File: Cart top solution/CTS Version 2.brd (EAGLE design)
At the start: 116.5 x 63 mm, 10 parts, among them T2 2N2222, U1 RASPBERRY_PI_40SMD, X1 CON-WAGO_740_740-102

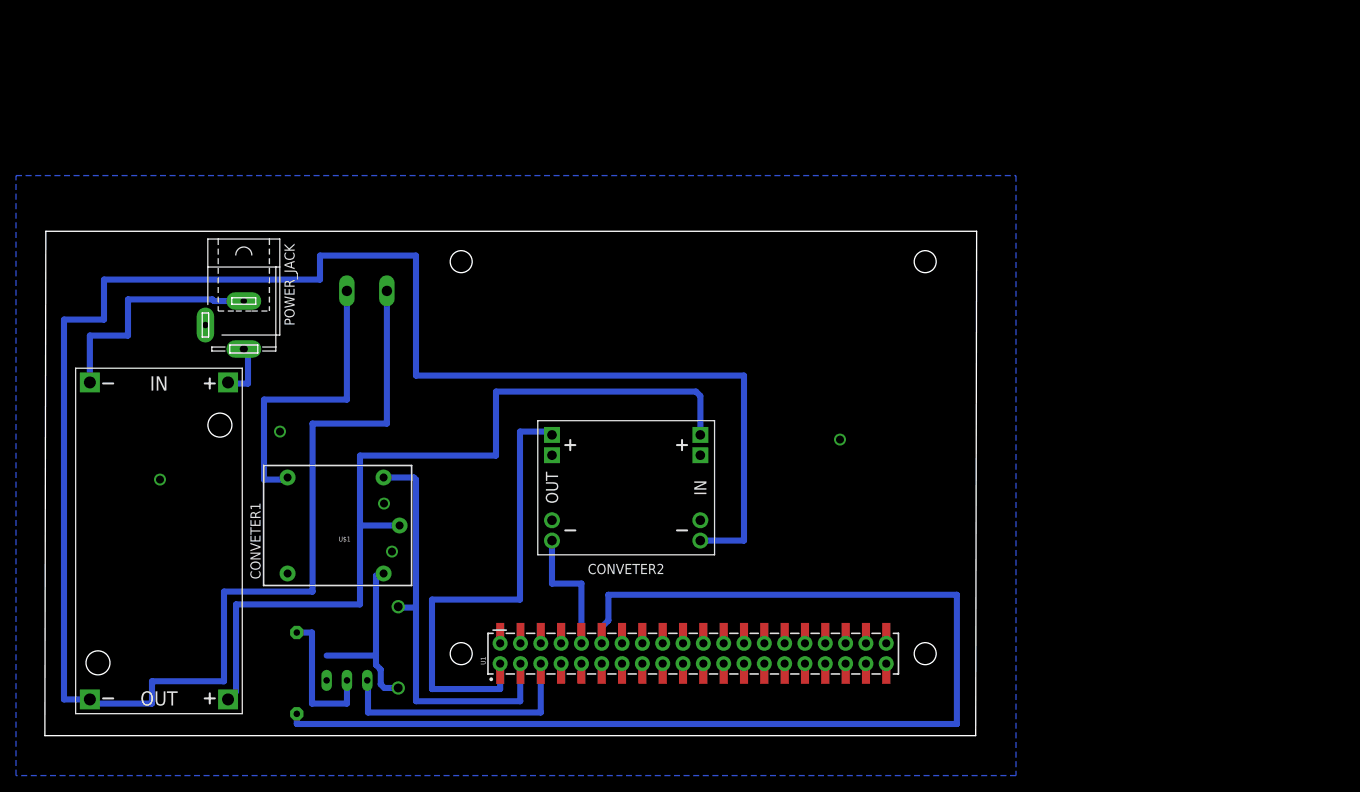
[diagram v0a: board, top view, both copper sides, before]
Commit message: Second Version of the Cart top solution circuit board. The updated board has been equiped with a real time clock module
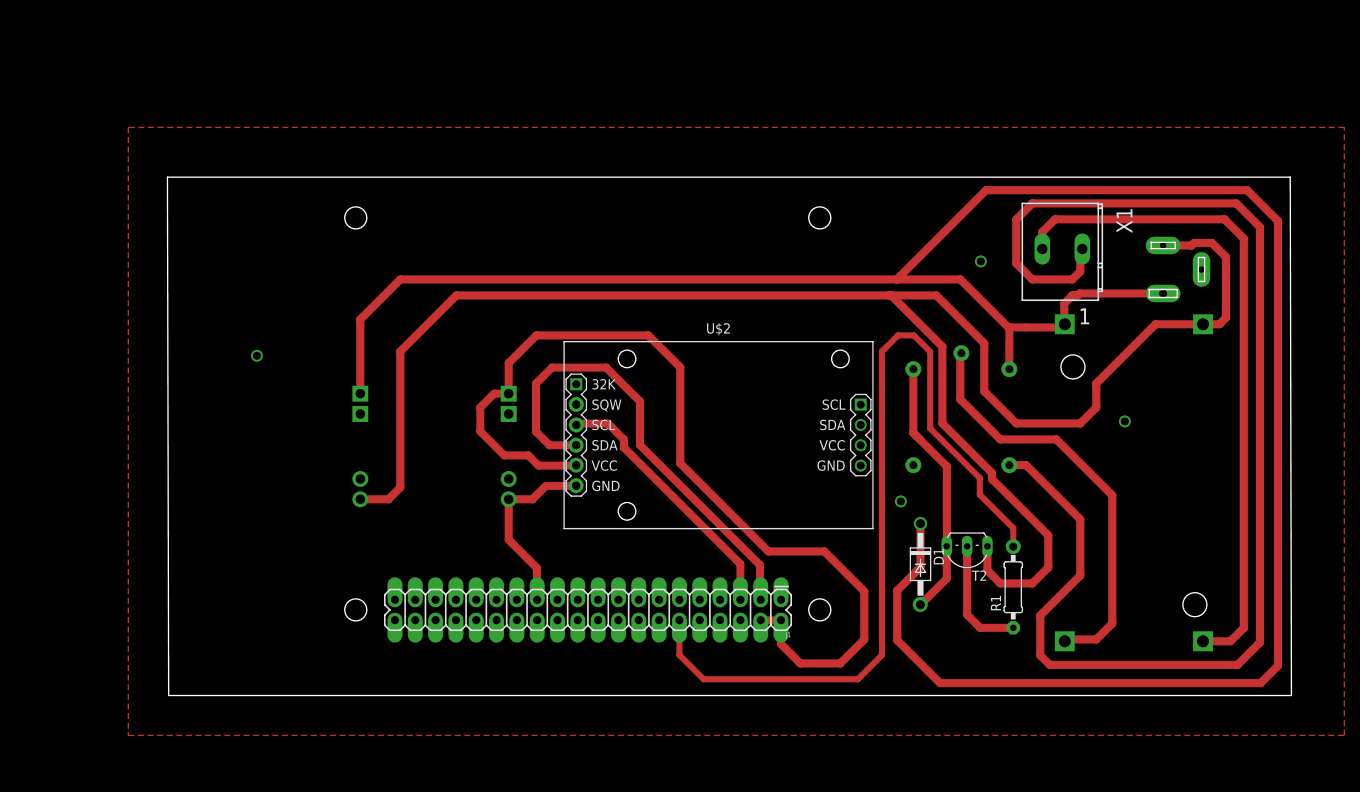
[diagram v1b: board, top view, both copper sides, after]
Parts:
- removed RASPBERRY_PI_CONECTOR: RASPBERRYPI-40-PIN-GPIO_PTH_NO_SHROUD, SparkFun-Connectors:2X20
- added J1: RASPBERRYPI-40-PIN-GPIO_PTH_NO_SHROUD, GHIISparkFun-Connectors:2X20
- added U$2: RTC-DS3231-AT24C32, GHIdiy-modules:RTC-DS3231-AT24C32
- moved CONVETER1 122.1 mm to (120.7, 26.6), flipped to the bottom
- moved POWER_JACK 115.1 mm to (124.4, 53.3), flipped to the bottom
- moved R1 90.2 mm to (105.7, 13.5), flipped to the top, turned to 90 degrees
- moved X1 87.1 mm to (111.8, 55.5), flipped to the top
- moved T2 79.3 mm to (99.9, 17.4), flipped to the top
- moved U$1 78.8 mm to (99.1, 35.4), flipped to the bottom, turned to 270 degrees
- moved D1 66.1 mm to (94.1, 16.4), flipped to the top
- moved U1 52.1 mm to (85.0, 5.94), flipped to the bottom
- moved CONVETER2 24.5 mm to (33.3, 31.1), flipped to the bottom
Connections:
- removed net N$10: CONVETER2.OUT-.1, RASPBERRY_PI_CONECTOR.9
- removed net N$3: CONVETER1.OUT-, CONVETER2.IN-.1, X1.L2
- removed net N$6: RASPBERRY_PI_CONECTOR.6, T2.E
- removed net N$9: D1.C, RASPBERRY_PI_CONECTOR.4, U$1.COIL0
- new net GND.2: U$2.J2.4
- new net N$4: CONVETER1.OUT-, X1.L2
- new net N$50: J1.5, U$2.J1.3
- new net VCC: CONVETER2.OUT+.2, J1.2, J1.4, U$2.J1.5
- new net VCC.2: U$2.J2.3
- net 3.3V: now also J1.1, J1.17; no longer RASPBERRY_PI_CONECTOR.1, RASPBERRY_PI_CONECTOR.17
- net GND: now also CONVETER2.OUT-.1, J1.14, J1.20, J1.25, J1.30, J1.34, J1.39, J1.6, J1.9, U$2.J1.6; no longer RASPBERRY_PI_CONECTOR.14, RASPBERRY_PI_CONECTOR.20, RASPBERRY_PI_CONECTOR.25, RASPBERRY_PI_CONECTOR.30, RASPBERRY_PI_CONECTOR.34, RASPBERRY_PI_CONECTOR.39
- net N$1: now also CONVETER2.IN+.2, D1.C, U$1.COIL0
- net N$13: no longer CONVETER2.IN+.2
- net N$2: now also J1.3, U$2.J1.4; no longer CONVETER1.IN-, POWER_JACK.1
- net N$5: now also CONVETER1.IN-, CONVETER2.IN-.1, POWER_JACK.1, T2.E; no longer CONVETER2.OUT+.2, RASPBERRY_PI_CONECTOR.2
- net N$7: now also J1.12; no longer RASPBERRY_PI_CONECTOR.11
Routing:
- net N$1: track 7.09 -> 298.8 mm
- net N$3: track 274.0 -> 0.00 mm
- net N$5: track 59.0 -> 216.7 mm
- net N$12: track 37.2 -> 161.9 mm
- net VCC: track 0.00 -> 115.2 mm
- net N$4: track 0.00 -> 83.4 mm
- net N$13: track 107.0 -> 52.7 mm
- net N$9: track 51.9 -> 0.00 mm
- net N$7: track 149.9 -> 106.5 mm
- net N$50: track 0.00 -> 32.9 mm, vias 0 -> 7
- net N$6: track 31.7 -> 0.00 mm
- net N$2: track 29.7 -> 58.4 mm
- net GND: track 0.00 -> 23.2 mm, vias 5 -> 4
- net N$10: track 16.5 -> 0.00 mm
- net N$8: track 23.6 -> 33.8 mm
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- added copper zone on layer 1, net GND
- removed copper zone on layer 16, net GND
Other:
- board size 116.5 x 63 mm -> 140.5 x 64.8 mm

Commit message: New version of the carttop solution board with an MCP3002 chip integrated
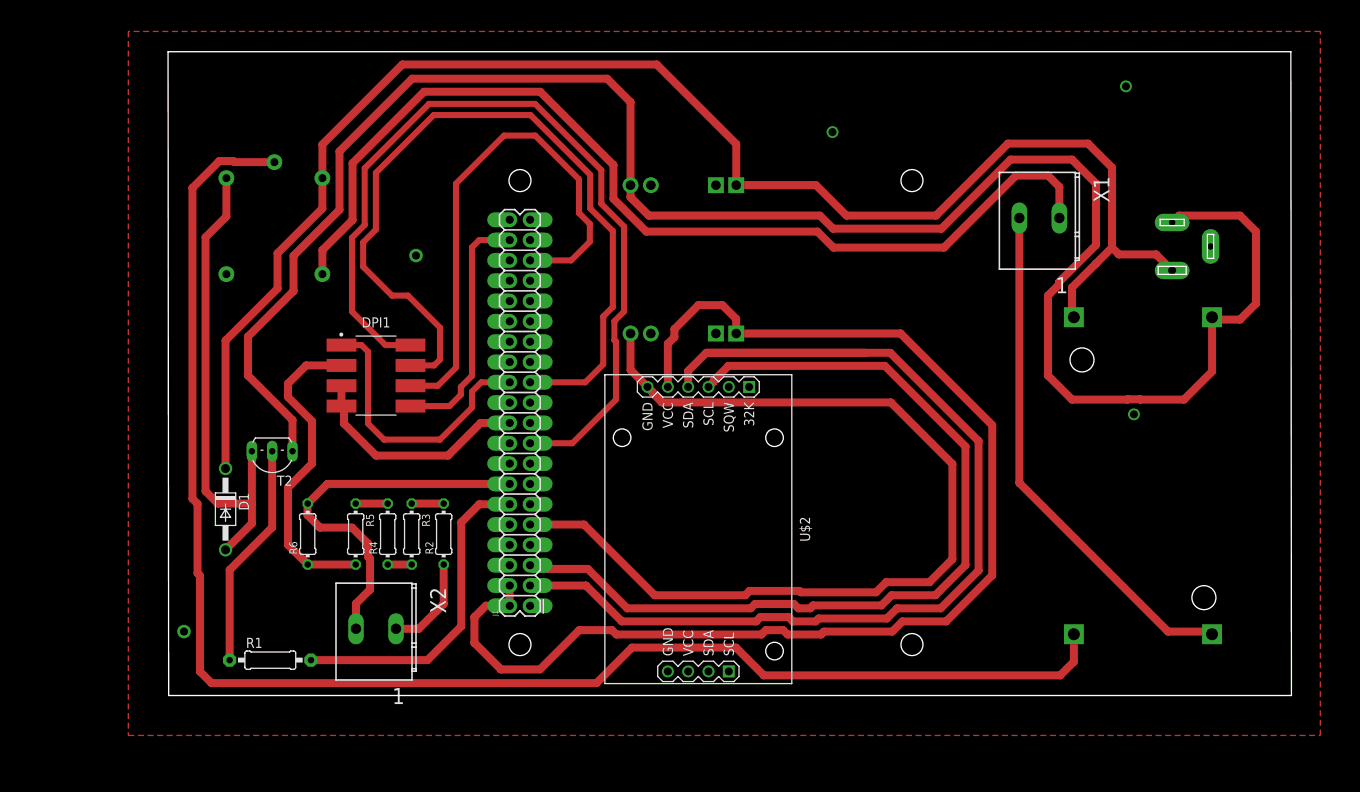
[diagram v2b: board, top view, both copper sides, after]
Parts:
- added DPI1: (no value), GHII MCP 3002:SOP254P1132X265-8N
- added R2, R3, R4, R5, R6: (no value), resistor:0204/7
- added X2: CON-WAGO_740_740-102, Termnal block:CON-WAGO_740_P-740-102
- moved R1 93.3 mm to (12.8, 4.43), turned to 0 degrees
- moved U$1 89.1 mm to (13.2, 59.3)
- moved T2 87.7 mm to (13.0, 29.3)
- moved D1 87.1 mm to (7.19, 23.3)
- moved U1 45.9 mm to (39.2, 2.86), turned to 90 degrees
- moved CONVETER2 38.9 mm to (64.4, 54.5), turned to 270 degrees
- moved J1 31.4 mm to (45.3, 11.2), turned to 90 degrees
- moved U$2 12.0 mm to (66.3, 20.8), turned to 270 degrees
- moved X1 4.83 mm to (108.9, 59.3)
- moved POWER_JACK 3.09 mm to (125.5, 56.1)
- moved CONVETER1 1.43 mm to (121.9, 27.5)
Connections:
- removed net 3.3V: J1.1, J1.17
- new net N$10: DPI1.8, J1.1, J1.17
- new net N$14: DPI1.1, J1.24
- new net N$16: R2.2, R3.1
- new net N$17: R3.2, R4.1
- new net N$18: R4.2, R5.1
- new net N$19: DPI1.2, R5.2, R6.1
- new net N$21: R2.1, X2.L1
- new net N$3: DPI1.7, J1.23
- new net N$6: DPI1.6, J1.35
- new net N$9: DPI1.5, J1.38
- net GND: now also DPI1.3, DPI1.4, R6.2, X2.L2
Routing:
- net GND: track 23.2 -> 197.8 mm, vias 4 -> 5
- net N$13: track 52.7 -> 189.8 mm
- net N$10: track 0.00 -> 109.6 mm
- net N$1: track 298.8 -> 193.8 mm
- net N$3: track 0.00 -> 101.5 mm
- net N$2: track 58.4 -> 141.0 mm
- net N$50: track 32.9 -> 111.6 mm, vias 7 -> 0
- net N$6: track 0.00 -> 66.6 mm
- net N$7: track 106.5 -> 40.5 mm
- net VCC: track 115.2 -> 157.2 mm
- net N$19: track 0.00 -> 39.8 mm
- net N$12: track 161.9 -> 126.2 mm
- net N$14: track 0.00 -> 35.3 mm
- net N$9: track 0.00 -> 31.0 mm
- net N$5: track 216.7 -> 246.2 mm
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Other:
- board size 140.5 x 64.8 mm -> 140.4 x 80.5 mm

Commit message: 2 sided board
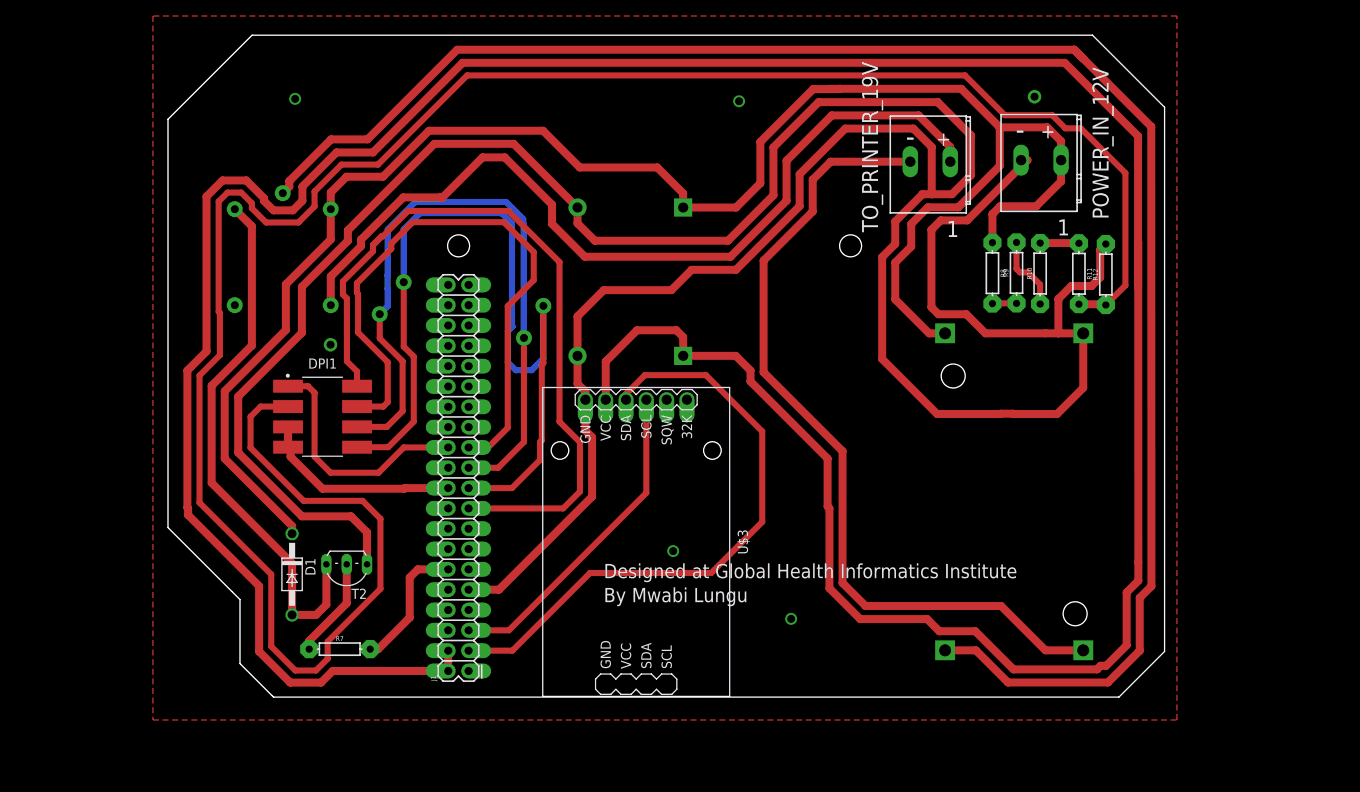
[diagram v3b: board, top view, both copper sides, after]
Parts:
- removed CONVETER2: DC-DC-STEP-DOWN-MP1584, GHIdiy-modules:DC-DC-STEP-DOWN-MP1584
- removed POWER_JACK: (no value), con-jack:SPC4077
- removed R1: (no value), adafruit:0207/10
- removed R2, R3, R4, R5, R6: (no value), resistor:0204/7
- removed X1, X2: CON-WAGO_740_740-102, Termnal block:CON-WAGO_740_P-740-102
- added POWER_IN_12V: Power in (12V), Termnal block:CON-WAGO_740_P-740-102
- added R10, R11, R12, R7, R8, R9: 1k, SparkFun-Resistors:AXIAL-0.3
- added TO_PRINTER_19V: CON-WAGO_740_740-102, Termnal block:CON-WAGO_740_P-740-102
- added U$3: RTC-DS3231-AT24C32, GHIdiy-modulesRTC:RTC-DS3231-AT24C32
- U$2: value RTC-DS3231-AT24C32 -> DC-DC-STEP-DOWN-MP1584; device GHIdiy-modules:RTC-DS3231-AT24C32 -> GHIdiy-modulesRTC:DC-DC-STEP-DOWN-MP1584
- moved U$2 32.1 mm to (57.8, 51.7), flipped to the bottom
- moved T2 16.9 mm to (22.3, 15.1)
- moved CONVETER1 16.2 mm to (105.8, 25.5)
- moved D1 11.6 mm to (15.5, 15.2)
- moved U1 11.2 mm to (31.5, -5.29)
- moved J1 11.2 mm to (37.6, 3.08)
- moved DPI1 8.43 mm to (19.3, 34.9)
- moved U$1 4.02 mm to (14.2, 55.4)
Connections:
- removed net GND.2: U$2.J2.4
- removed net N$16: R2.2, R3.1
- removed net N$17: R3.2, R4.1
- removed net N$18: R4.2, R5.1
- removed net N$21: R2.1, X2.L1
- removed net VCC.2: U$2.J2.3
- new net N$15: R10.P$1, R9.P$2
- new net N$20: R10.P$2, R11.P$1
- net GND: now also CONVETER1.IN-, POWER_IN_12V.L2, R12.P$2, T2.E, U$2.IN-.1, U$2.OUT-.1, U$3.J1.6; no longer CONVETER2.OUT-.1, R6.2, U$2.J1.6, X2.L2
- net N$1: now also POWER_IN_12V.L1, R8.P$1, U$2.IN+.2; no longer CONVETER2.IN+.2, POWER_JACK.3
- net N$11: now also R7.P$1; no longer R1.1
- net N$12: now also TO_PRINTER_19V.L1; no longer X1.L1
- net N$19: now also R11.P$2, R12.P$1; no longer R5.2, R6.1
- net N$2: now also U$3.J1.4; no longer U$2.J1.4
- net N$4: now also TO_PRINTER_19V.L2; no longer X1.L2
- net N$5: now also R8.P$2, R9.P$1; no longer CONVETER1.IN-, CONVETER2.IN-.1, POWER_JACK.1, T2.E
- net N$50: now also U$3.J1.3; no longer U$2.J1.3
- net N$6: now also J1.21; no longer J1.35
- net N$7: now also R7.P$2; no longer R1.2
- net N$9: now also J1.19; no longer J1.38
- net VCC: now also U$2.OUT+.2, U$3.J1.5; no longer CONVETER2.OUT+.2, U$2.J1.5
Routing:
- net N$5: track 246.2 -> 3.02 mm
- net VCC: track 157.2 -> 393.2 mm
- net N$19: track 39.8 -> 269.0 mm
- net GND: track 197.8 -> 425.3 mm, vias 5 -> 6
- net N$9: track 31.0 -> 107.4 mm, vias 0 -> 2
- net N$50: track 111.6 -> 41.0 mm
- net N$2: track 141.0 -> 76.3 mm
- net N$4: track 65.0 -> 103.7 mm
- net N$1: track 193.8 -> 221.6 mm
- net N$13: track 189.8 -> 215.4 mm
- net N$3: track 101.5 -> 76.9 mm
- net N$7: track 40.5 -> 16.8 mm
- net N$6: track 66.6 -> 86.3 mm, vias 0 -> 2
- net N$12: track 126.2 -> 108.3 mm
- net N$11: track 28.3 -> 12.5 mm
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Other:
- board size 140.4 x 80.5 mm -> 124.6 x 82.7 mm
- board text added: "+"
- board text added: "-"
- board text added: "By Mwabi Lungu"
- board text added: "Designed at Global Health Informatics Institute"
